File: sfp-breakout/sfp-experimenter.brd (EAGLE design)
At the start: 65 x 65 mm, 49 parts, among them IC1 SN65LVDS1DBV, IC2 SN65LVDT2DBV, J1 694108106102, T1 BC847, T2 BC847, U1 LDO-MCP1825S, X1 PINHD-1X5LOCK, X2 PINHD-1X5LOCK, X3 PINHD-1X4LOCK

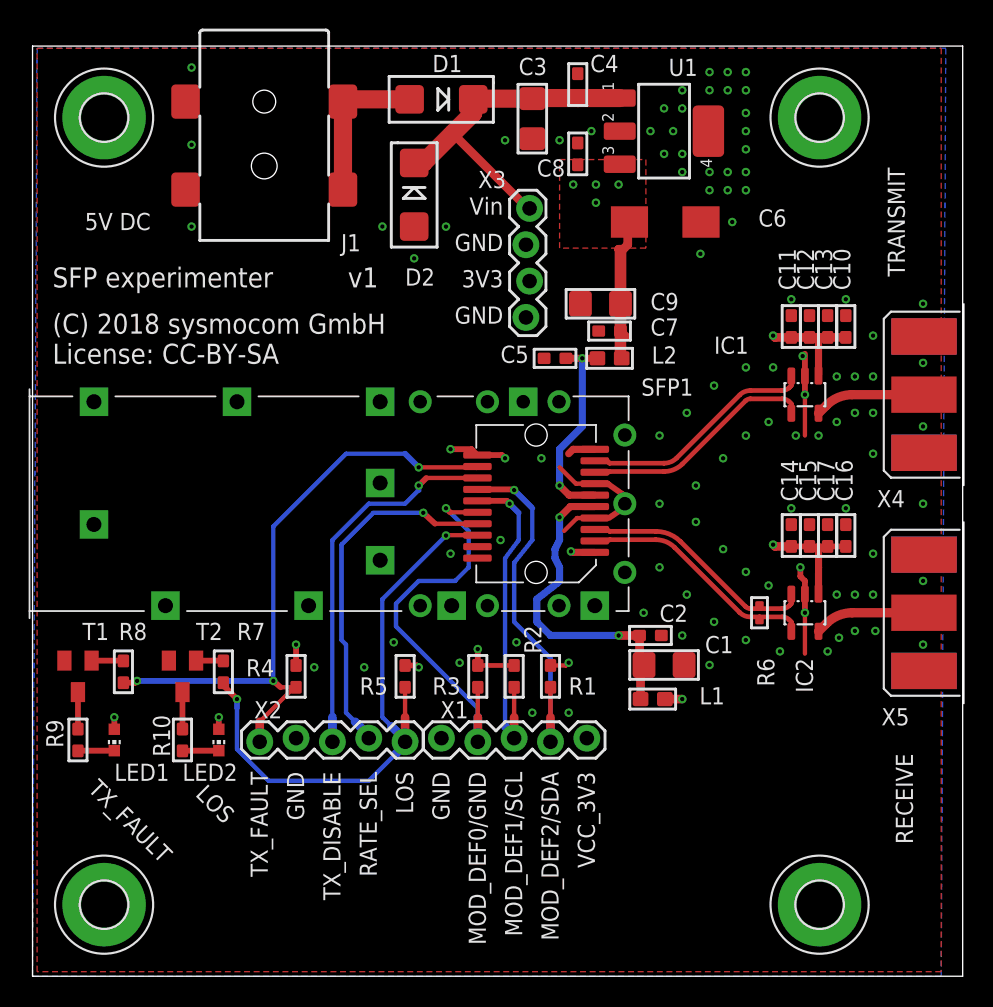
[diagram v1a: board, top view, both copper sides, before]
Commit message: sfp-*: add OSHW logo, fill ext'd attribs for BOM
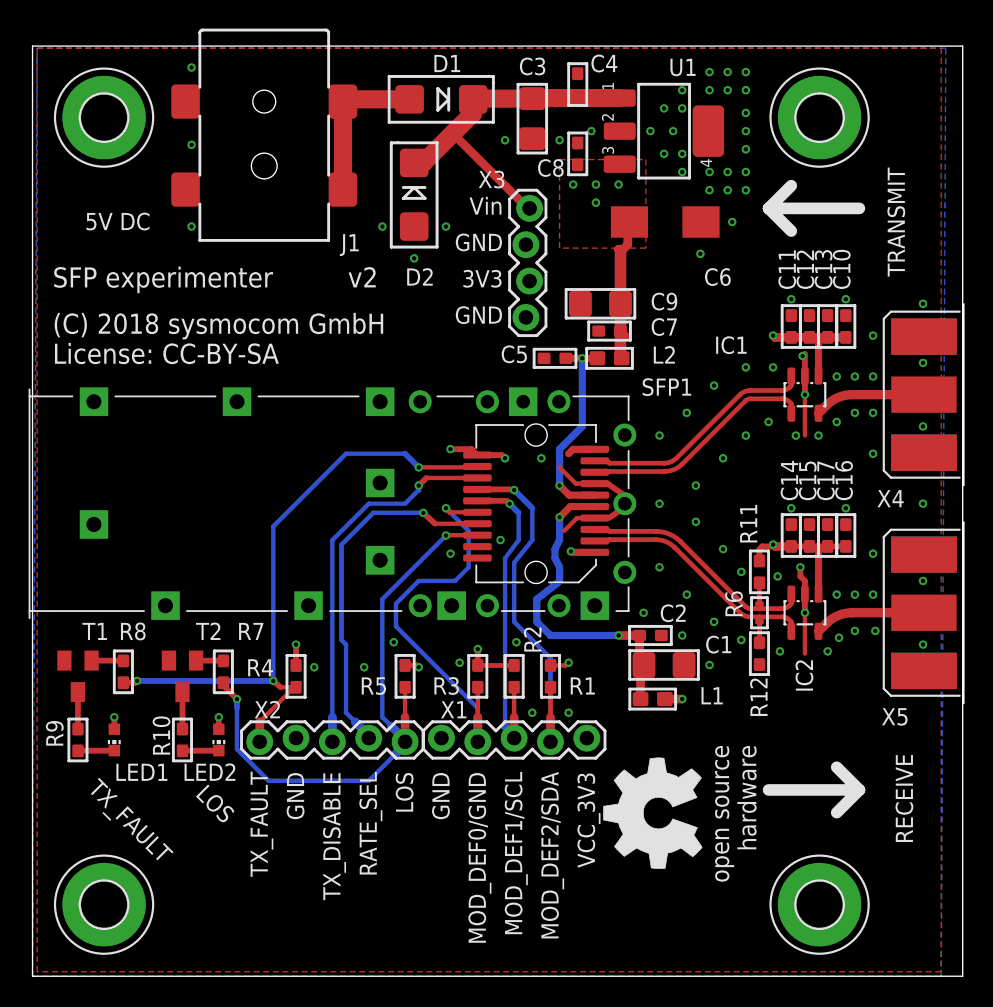
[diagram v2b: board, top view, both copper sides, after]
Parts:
- added R11: DNP, sfp-experimenter:_0603
- added R12: 100k, rc-sysmocom:_0603
- added U$1: (no value), oshw:OSHW_8MM
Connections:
- net GND: now also R12.2
- net RD_N: now also R12.1
- net RD_P: now also R11.2
- net VCC_3V3: now also R11.1
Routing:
- net VCC_3V3: track 37.5 -> 39.5 mm
- net RD_P: track 16.8 -> 18.4 mm
- net RD_N: track 16.8 -> 18.4 mm

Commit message: sfp-experimenter: update ext'd attribs and BOM
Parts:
- J1: value 694108106102 -> PJ-002BH-SMT-TR

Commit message: sfp-experimenter: update ext BOM attr to newer Digikey format
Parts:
- D1: value SS16T3G -> STPS2L60A
- IC2: value SN65LVDT2DBV -> PI90LV02TEX
- R12: value 100k -> DNP
- R6: value DNP -> 110R
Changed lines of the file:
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@@
 <attribute name="DATASHEET" value="https://www.samsungsem.com/kr/support/product-search/mlcc/CL31A106KOHNNNE.jsp" x="39.6875" y="46.99" size="1.778" layer="27" display="off"/>
 </element>
-<element name="IC2" library="sfp-experimenter" package="SOT23-5" value="SN65LVDT2DBV" x="53.975" y="25.4" smashed="yes" rot="R180">
+<element name="IC2" library="sfp-experimenter" package="SOT23-5" value="PI90LV02TEX" x="53.975" y="25.4" smashed="yes" rot="R180">
 <attribute name="NAME" x="53.34" y="22.225" size="1.2" layer="25" ratio="16" rot="R270"/>
 <attribute name="VALUE" x="55.88" y="28.829" size="1.27" layer="27" rot="R180"/>
 <attribute name="DESCRIPTION" value="IC RECEIVER 0/1 SOT23-5" x="53.975" y="25.4" size="1.778" layer="27" rot="R180" display="off"/>
-<attribute name="MANUFACTURER" value="Texas Instruments" x="53.975" y="25.4" size="1.778" layer="27" rot="R180" display="off"/>
-<attribute name="MANUFACTURERPARTNUMBER" value="SN65LVDT2DBVR" x="53.975" y="25.4" size="1.778" layer="27" rot="R180" display="off"/>
+<attribute name="MANUFACTURER" value="Diodes Incorporated" x="53.975" y="25.4" size="1.778" layer="27" rot="R180" display="off"/>
+<attribute name="MANUFACTURERPARTNUMBER" value="PI90LV02TEX" x="53.975" y="25.4" size="1.778" layer="27" rot="R180" display="off"/>
 <attribute name="SOURCE" value="DIGIKEY" x="53.975" y="25.4" size="1.778" layer="27" rot="R180" display="off"/>
-<attribute name="SOURCEPARTNUMBER" value="296-6896-1-ND" x="53.975" y="25.4" size="1.778" layer="27" rot="R180" display="off"/>
+<attribute name="SOURCEPARTNUMBER" value="PI90LV02TEXCT-ND" x="53.975" y="25.4" size="1.778" layer="27" rot="R180" display="off"/>
 <attribute name="ROHSCERTIFICATE" value="ROHS3 Compliant" x="53.975" y="25.4" size="1.778" layer="27" rot="R180" display="off"/>
 <attribute name="POPULATED" value="TRUE" x="53.975" y="25.4" size="1.778" layer="27" rot="R180" display="off"/>
 <attribute name="CLASS" value="IC" x="53.975" y="25.4" size="1.778" layer="27" rot="R180" display="off"/>
-<attribute name="LINK" value="https://www.digikey.com/product-detail/en/texas-instruments/SN65LVDT2DBVR/296-6896-1-ND/371534" x="53.975" y="25.4" size="1.778" layer="27" rot="R180" display="off"/>
-<attribute name="DATASHEET" value="http://www.ti.com/general/docs/suppproductinfo.tsp?distId=10&amp;gotoUrl=http%3A%2F%2Fwww.ti.com%2Flit%2Fgpn%2Fsn65lvds1" x="53.975" y="25.4" size="1.778" layer="27" rot="R180" display="off"/>
+<attribute name="LINK" value="https://www.digikey.com/en/products/detail/diodes-incorporated/PI90LV02TEX/1142813" x="53.975" y="25.4" size="1.778" layer="27" rot="R180" display="off"/>
+<attribute name="DATASHEET" value="https://www.diodes.com/assets/Datasheets/PI90LV02.pdf" x="53.975" y="25.4" size="1.778" layer="27" rot="R180" display="off"/>
 </element>
 <element name="IC1" library="sfp-experimenter" package="SOT23-5" value="SN65LVDS1DBV" x="53.975" y="40.64" smashed="yes" rot="R180">
@@
 <attribute name="DATASHEET" value="https://ww1.microchip.com/downloads/en/DeviceDoc/22056b.pdf" x="44.1325" y="59.055" size="1.778" layer="27" rot="R270" display="off"/>
 </element>
-<element name="D1" library="sfp-experimenter" package="SMADIODE" value="SS16T3G" x="28.575" y="61.2775" smashed="yes" rot="R180">
+<element name="D1" library="sfp-experimenter" package="SMADIODE" value="STPS2L60A" x="28.575" y="61.2775" smashed="yes" rot="R180">
 <attribute name="NAME" x="27.94" y="63.1825" size="1.2" layer="25" font="vector" ratio="16"/>
 <attribute name="VALUE" x="31.115" y="63.5635" size="0.4064" layer="27" font="vector" ratio="10" rot="R180"/>
@@
 <attribute name="DATASHEET" value="https://www.bourns.com/docs/Product-Datasheets/SMAJ.pdf" x="26.67" y="54.61" size="1.778" layer="27" rot="R270" display="off"/>
 </element>
-<element name="R6" library="sfp-experimenter" package="_0402" value="DNP" x="50.8" y="25.4" smashed="yes" rot="R270">
-<attribute name="DESCRIPTION" value="NO DESCRIPTION" x="50.8" y="25.4" size="1.778" layer="27" rot="R270" display="off"/>
-<attribute name="MANUFACTURER" value="UNKNOWN MANUFACTURER" x="50.8" y="25.4" size="1.778" layer="27" rot="R270" display="off"/>
-<attribute name="MANUFACTURERPARTNUMBER" value="UNKNOWN MANUFACTURER PART NUMBER" x="50.8" y="25.4" size="1.778" layer="27" rot="R270" display="off"/>
-<attribute name="SOURCE" value="UNKNOWN SOURCE" x="50.8" y="25.4" size="1.778" layer="27" rot="R270" display="off"/>
-<attribute name="SOURCEPARTNUMBER" value="UNKNOWN SOURCE PART NUMBER" x="50.8" y="25.4" size="1.778" layer="27" rot="R270" display="off"/>
-<attribute name="ROHSCERTIFICATE" value="UNKNOWN ROHS CERTIFICATE" x="50.8" y="25.4" size="1.778" layer="27" rot="R270" display="off"/>
-<attribute name="POPULATED" value="FALSE" x="50.8" y="25.4" size="1.778" layer="27" rot="R270" display="off"/>
+<element name="R6" library="sfp-experimenter" package="_0402" value="110R" x="50.8" y="25.4" smashed="yes" rot="R270">
+<attribute name="DESCRIPTION" value="RES 110 OHM 1% 1/10W 0603" x="50.8" y="25.4" size="1.778" layer="27" rot="R270" display="off"/>
+<attribute name="MANUFACTURER" value="YAGEO" x="50.8" y="25.4" size="1.778" layer="27" rot="R270" display="off"/>
+<attribute name="MANUFACTURERPARTNUMBER" value="RC0603FR-13110RL" x="50.8" y="25.4" size="1.778" layer="27" rot="R270" display="off"/>
+<attribute name="SOURCE" value="DIGIKEY" x="50.8" y="25.4" size="1.778" layer="27" rot="R270" display="off"/>
+<attribute name="SOURCEPARTNUMBER" value="13-RC0603FR-13110RLCT-ND" x="50.8" y="25.4" size="1.778" layer="27" rot="R270" display="off"/>
+<attribute name="ROHSCERTIFICATE" value="ROHS3 Compliant" x="50.8" y="25.4" size="1.778" layer="27" rot="R270" display="off"/>
+<attribute name="POPULATED" value="TRUE" x="50.8" y="25.4" size="1.778" layer="27" rot="R270" display="off"/>
 <attribute name="CLASS" value="RESISTOR" x="50.8" y="25.4" size="1.778" layer="27" rot="R270" display="off"/>
-<attribute name="LINK" value="UNKNOWN LINK" x="50.8" y="25.4" size="1.778" layer="27" rot="R270" display="off"/>
+<attribute name="LINK" value="https://www.digikey.com/en/products/detail/yageo/RC0603FR-13110RL/14286378" x="50.8" y="25.4" size="1.778" layer="27" rot="R270" display="off"/>
 <attribute name="NAME" x="48.4189" y="26.9875" size="1.2" layer="25" font="vector" ratio="16" rot="R270"/>
 <attribute name="VALUE" x="49.4664" y="26.67" size="0.508" layer="27" font="vector" ratio="10" rot="R270"/>
+<attribute name="DATASHEET" value="https://www.yageo.com/upload/media/product/productsearch/datasheet/rchip/PYu-RC_Group_51_RoHS_L_12.pdf" x="50.8" y="25.4" size="1.778" layer="27" rot="R270" display="off"/>
 </element>
 <element name="X3" library="sfp-experimenter" package="1X04_LOCK" value="PINHD-1X4LOCK" x="34.6075" y="53.6575" smashed="yes" rot="R270">
@@
 <attribute name="VALUE" x="27.305" y="19.685" size="1.27" layer="27" ratio="10" rot="R180"/>
 </element>
-<element name="R12" library="rc-sysmocom" package="_0603" value="100k" x="50.8" y="22.5425" smashed="yes" rot="R270">
+<element name="R12" library="rc-sysmocom" package="_0603" value="DNP" x="50.8" y="22.5425" smashed="yes" rot="R270">
 <attribute name="NAME" x="50.165" y="20.955" size="1.2" layer="25" font="vector" ratio="16" rot="R270"/>
 <attribute name="VALUE" x="49.3077" y="24.13" size="0.508" layer="27" font="vector" ratio="10" rot="R270"/>
@@
 <attribute name="SOURCEPARTNUMBER" value="2019-RK73H1JTTD1003FCT-ND" x="50.8" y="22.5425" size="1.778" layer="27" rot="R270" display="off"/>
 <attribute name="ROHSCERTIFICATE" value="ROHS3 Compliant" x="50.8" y="22.5425" size="1.778" layer="27" rot="R270" display="off"/>
-<attribute name="POPULATED" value="TRUE" x="50.8" y="22.5425" size="1.778" layer="27" rot="R270" display="off"/>
+<attribute name="POPULATED" value="FALSE" x="50.8" y="22.5425" size="1.778" layer="27" rot="R270" display="off"/>
 <attribute name="CLASS" value="RESISTOR" x="50.8" y="22.5425" size="1.778" layer="27" rot="R270" display="off"/>
 <attribute name="LINK" value="https://www.digikey.com/product-detail/en/koa-speer-electronics-inc/RK73H1JTTD1003F/2019-RK73H1JTTD1003FCT-ND/9846889" x="50.8" y="22.5425" size="1.778" layer="27" rot="R270" display="off"/>

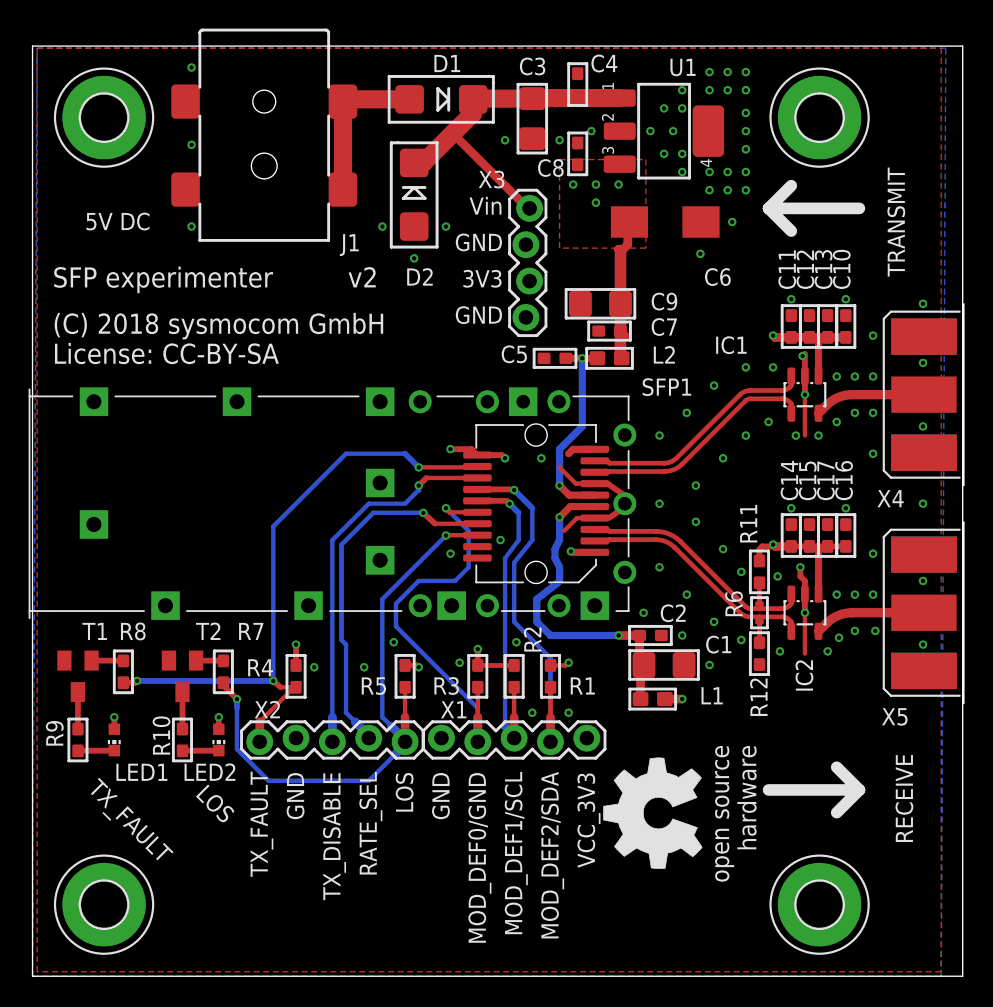
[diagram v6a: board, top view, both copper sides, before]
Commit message: sfp-experimenter: insert main fiducials
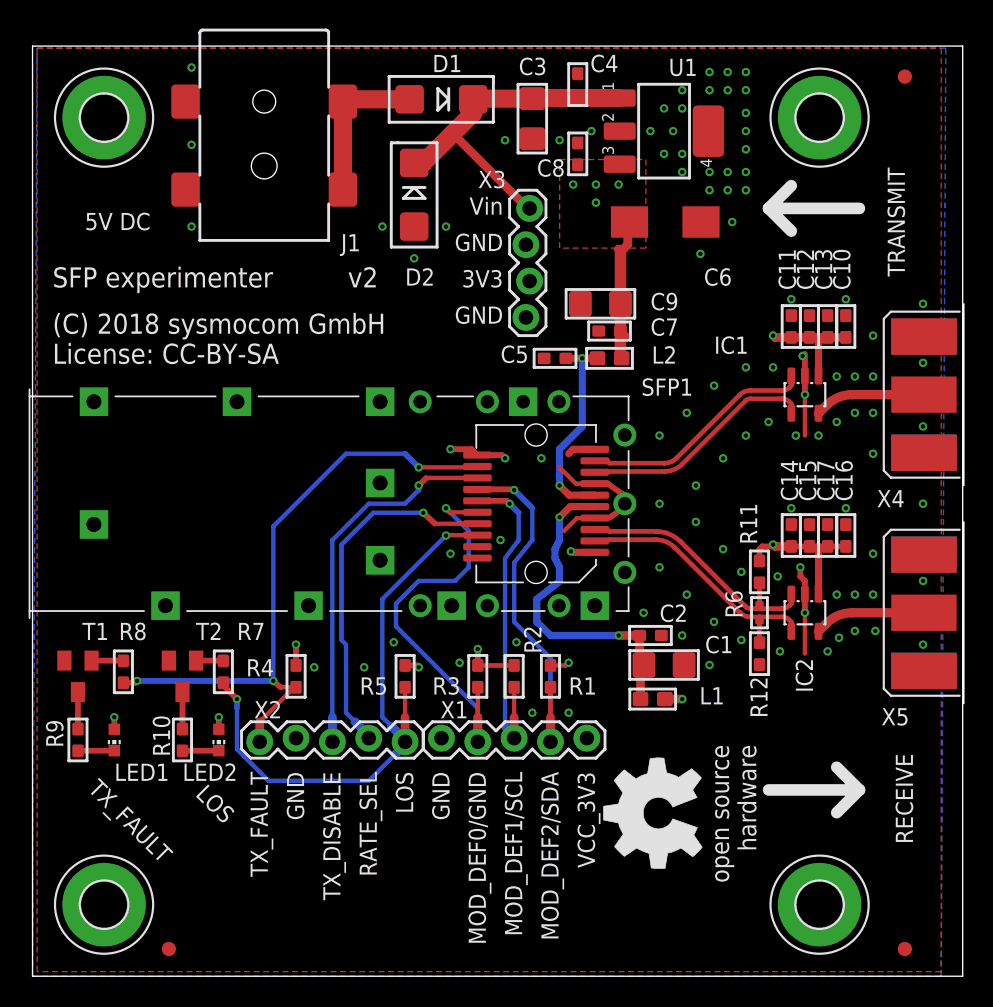
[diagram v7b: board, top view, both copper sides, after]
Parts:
- added FID1, FID2, FID3: FIDUCIAL1X2.5, microbuilder:FIDUCIAL-1X2.5
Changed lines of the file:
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@@
 <setting verticaltext="up"/>
 </settings>
-<grid distance="0.3175" unitdist="mm" unit="mm" style="lines" multiple="1" display="no" altdistance="0.15875" altunitdist="mm" altunit="mm"/>
+<grid distance="2.54" unitdist="mm" unit="mm" style="lines" multiple="1" display="yes" altdistance="1.27" altunitdist="mm" altunit="mm"/>
 <layers>
 <layer number="1" name="Top" color="4" fill="1" visible="yes" active="yes"/>
@@
 <layer number="99" name="position" color="7" fill="9" visible="no" active="no"/>
 <layer number="100" name="Muster" color="7" fill="1" visible="no" active="no"/>
+<layer number="101" name="Patch_Top" color="12" fill="4" visible="yes" active="yes"/>
+<layer number="102" name="Mittellin" color="7" fill="1" visible="yes" active="yes"/>
+<layer number="103" name="Stiffner" color="7" fill="1" visible="yes" active="yes"/>
+<layer number="104" name="Name" color="7" fill="1" visible="yes" active="yes"/>
 <layer number="105" name="Beschreib" color="9" fill="1" visible="no" active="no"/>
 <layer number="106" name="BGA-Top" color="4" fill="1" visible="no" active="no"/>
 <layer number="107" name="BD-Top" color="5" fill="1" visible="no" active="no"/>
+<layer number="108" name="tBridges" color="7" fill="1" visible="yes" active="yes"/>
+<layer number="109" name="tBPL" color="7" fill="1" visible="yes" active="yes"/>
+<layer number="110" name="bBPL" color="7" fill="1" visible="yes" active="yes"/>
+<layer number="111" name="MPL" color="7" fill="1" visible="yes" active="yes"/>
 <layer number="112" name="Laser Beschriftung-2" color="15" fill="0" visible="no" active="no"/>
 <layer number="113" name="Laser Schnitt" color="12" fill="1" visible="no" active="no"/>
@@
 <layer number="115" name="Laser Bohrungen" color="9" fill="1" visible="no" active="no"/>
 <layer number="118" name="Rect_Pads" color="7" fill="1" visible="no" active="no"/>
+<layer number="121" name="sName" color="7" fill="1" visible="yes" active="yes"/>
+<layer number="122" name="_bPlace" color="7" fill="1" visible="yes" active="yes"/>
+<layer number="125" name="_tNames" color="7" fill="1" visible="yes" active="yes"/>
+<layer number="126" name="_bNames" color="7" fill="1" visible="yes" active="yes"/>
+<layer number="127" name="_tValues" color="7" fill="1" visible="yes" active="yes"/>
+<layer number="128" name="_bValues" color="7" fill="1" visible="yes" active="yes"/>
 <layer number="133" name="Ritzung" color="1" fill="0" visible="no" active="no"/>
 <layer number="134" name="Fräsung" color="2" fill="0" visible="no" active="no"/>
 <layer number="142" name="BMRestrict" color="1" fill="9" visible="no" active="no"/>
+<layer number="144" name="Drill_legend" color="7" fill="1" visible="yes" active="yes"/>
 <layer number="148" name="Document_mirrored" color="7" fill="1" visible="no" active="no"/>
+<layer number="151" name="HeatSink" color="7" fill="1" visible="yes" active="yes"/>
+<layer number="152" name="_bDocu" color="7" fill="1" visible="yes" active="yes"/>
 <layer number="156" name="gesam-Maß" color="1" fill="7" visible="no" active="no"/>
 <layer number="157" name="FaceMchng" color="3" fill="1" visible="no" active="no"/>
@@
 <layer number="223" name="223bmp" color="24" fill="1" visible="no" active="no"/>
 <layer number="224" name="224bmp" color="25" fill="1" visible="no" active="no"/>
+<layer number="248" name="Housing" color="7" fill="1" visible="yes" active="yes"/>
+<layer number="249" name="Edge" color="7" fill="1" visible="yes" active="yes"/>
 <layer number="250" name="Descript" color="3" fill="1" visible="no" active="no"/>
 <layer number="251" name="SMDround" color="12" fill="11" visible="no" active="no"/>
+<layer number="254" name="cooling" color="7" fill="1" visible="yes" active="yes"/>
 </layers>
 <board>
@@
 </element>
 <element name="U$1" library="oshw" package="OSHW_8MM" value="" x="43.745" y="11.3725" rot="R90"/>
+<element name="FID1" library="microbuilder" package="FIDUCIAL-1X2.5" value="FIDUCIAL1X2.5" x="9.525" y="1.905">
+<attribute name="BOM" value="EXCLUDE" x="9.525" y="1.905" size="1.778" layer="27" display="off"/>
+</element>
+<element name="FID2" library="microbuilder" package="FIDUCIAL-1X2.5" value="FIDUCIAL1X2.5" x="60.96" y="62.865">
+<attribute name="BOM" value="EXCLUDE" x="60.96" y="62.865" size="1.778" layer="27" display="off"/>
+</element>
+<element name="FID3" library="microbuilder" package="FIDUCIAL-1X2.5" value="FIDUCIAL1X2.5" x="60.96" y="1.905">
+<attribute name="BOM" value="EXCLUDE" x="60.96" y="1.905" size="1.778" layer="27" display="off"/>
+</element>
 </elements>
 <signals>
